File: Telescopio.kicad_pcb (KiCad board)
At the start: 2 copper layers, 201.9 x 119.4 mm, 18 parts, among them CON1 BARREL_JACK, P1 CONN_01X03, P10 CONN_01X08, P12 CONN_01X04, P13 CONN_01X04, P2 CONN_01X03, P3 CONN_01X05, P4 CONN_01X19, P5 CONN_01X19, P50 CONN_01X04, P51 CONN_01X10, P7 CONN_01X08, P8 CONN_01X08, P9 CONN_01X08

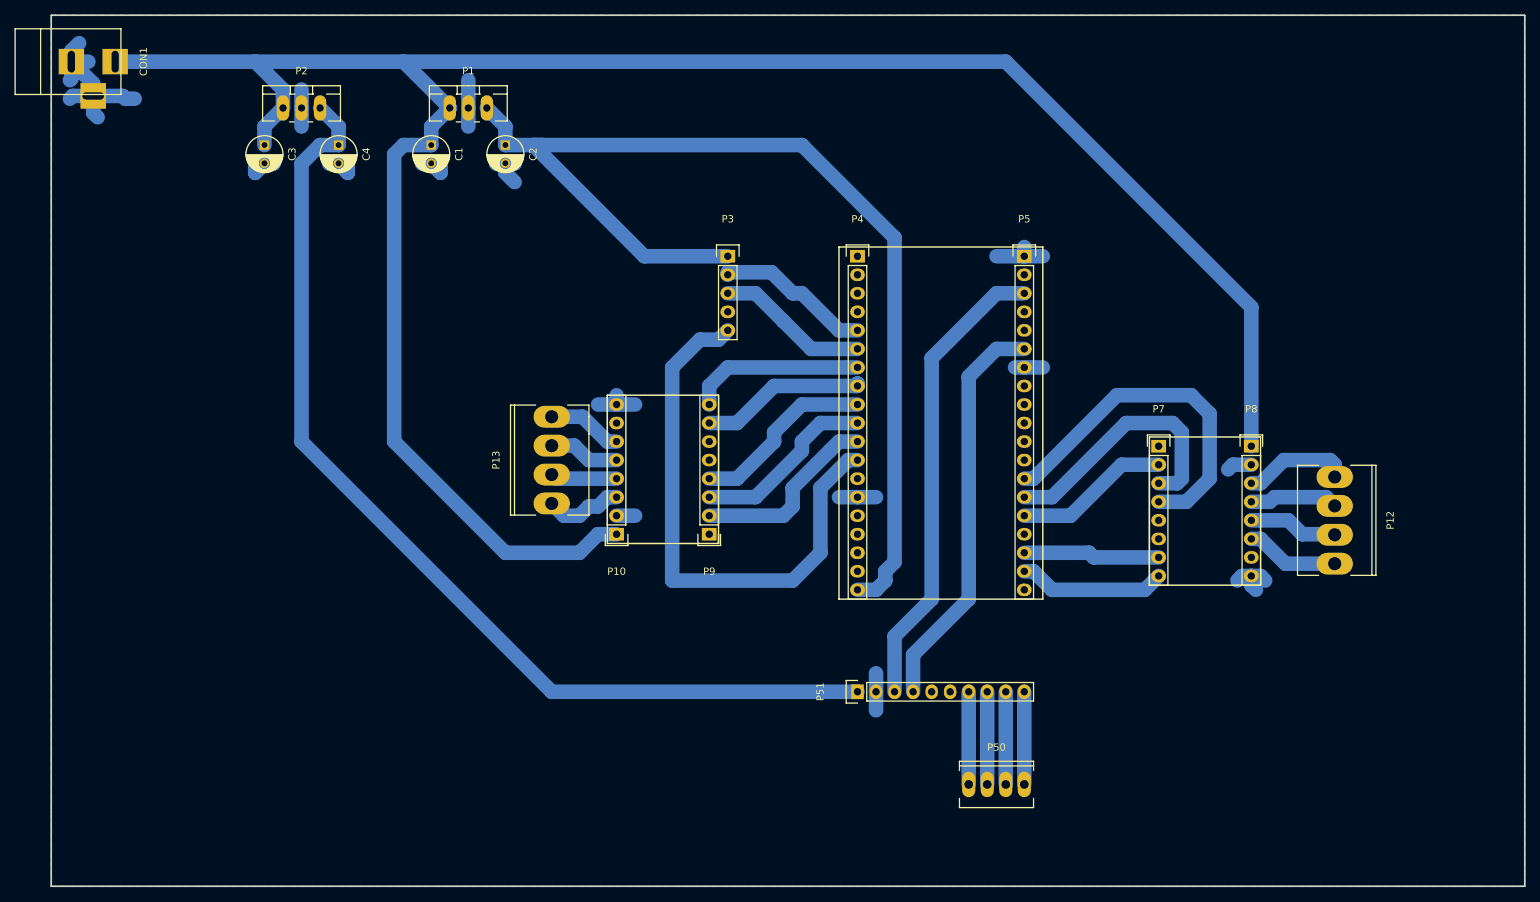
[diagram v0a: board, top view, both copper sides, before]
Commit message: button reset
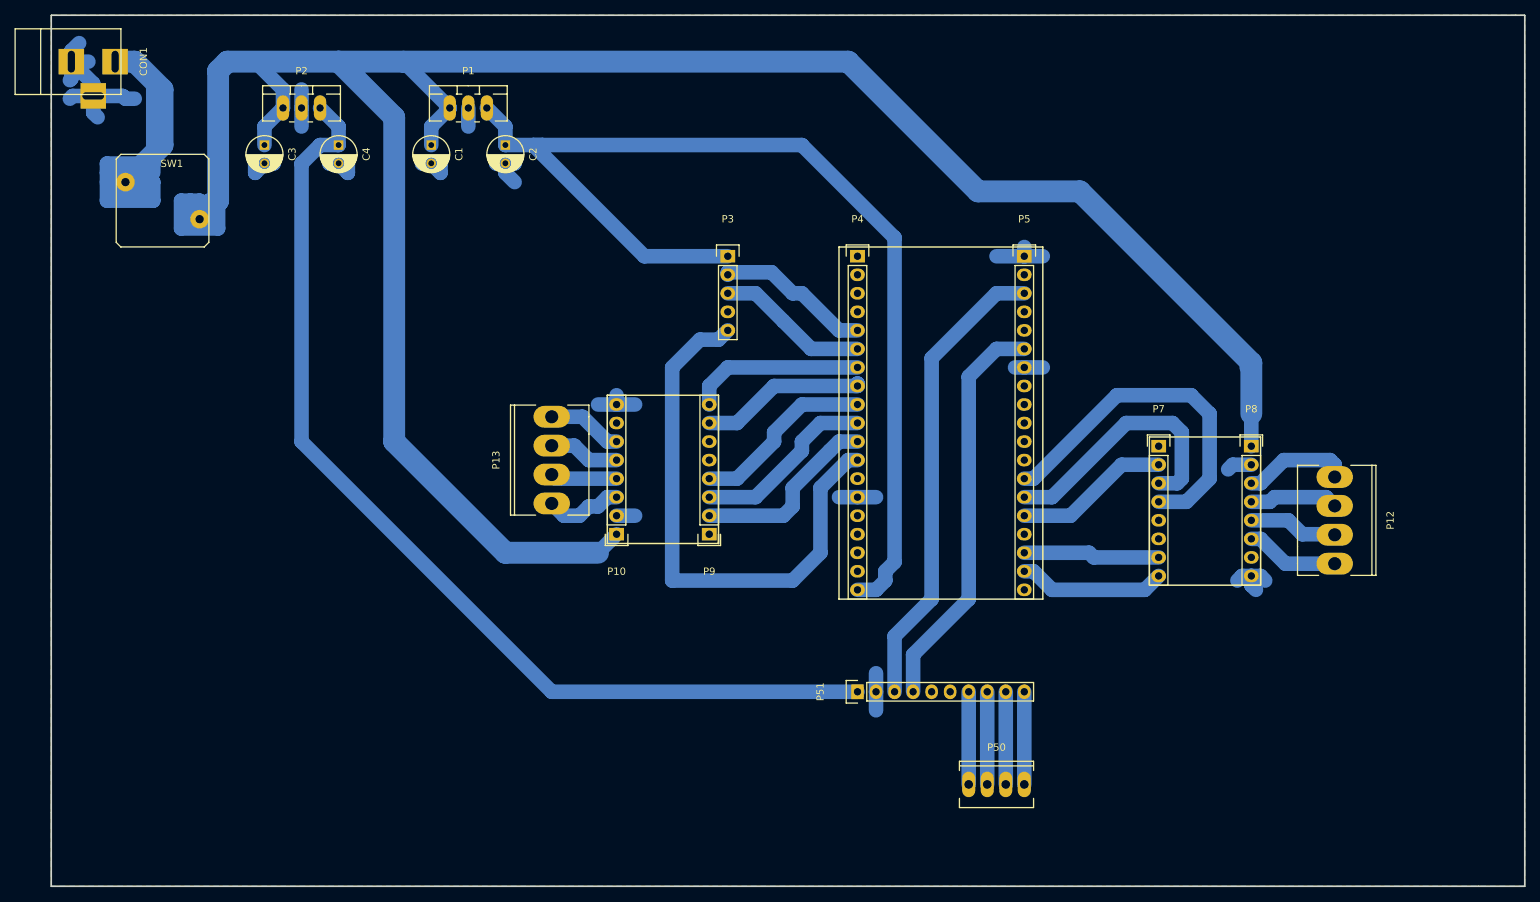
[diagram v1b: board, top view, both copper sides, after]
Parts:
- added SW1: SW_PUSH, Buttons_Switches_ThroughHole:SW_PUSH, F.Cu at (35.6, 53.3)
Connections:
- C1 pad 1: /24v -> /24v_Sal
- C3 pad 1: /24v -> /24v_Sal
- P1 pad 1: /24v -> /24v_Sal
- P10 pad 1: /24v -> /24v_Sal
- P2 pad 1: /24v -> /24v_Sal
- P8 pad 1: /24v -> /24v_Sal
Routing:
- net /24v_Sal: track 0.00 -> 373.3 mm
- net /24v: track 300.7 -> 80.6 mm
- net GND: track 100.8 -> 97.0 mm

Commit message: modifed pcb for testing
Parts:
- removed C1, C2, C3, C4: C, Capacitors_ThroughHole:C_Radial_D5_L11_P2.5
- removed CON1: BARREL_JACK, Connect:BARREL_JACK
- removed P1, P2: CONN_01X03, TO_SOT_Packages_THT:TO-220_Neutral123_Vertical_LargePads
- removed P10, P7, P8, P9: CONN_01X08, Pin_Headers:Pin_Header_Straight_1x08
- removed P12, P13: CONN_01X04, Sockets_MOLEX_KK-System:Socket_MOLEX-KK-RM3-96mm_Lock_4pin_straight
- removed P3: CONN_01X05, Pin_Headers:Pin_Header_Straight_1x05
- removed P50: CONN_01X04, Sockets_MOLEX_KK-System:Socket_MOLEX-KK-RM2-54mm_Lock_4pin_straight
- removed P51: CONN_01X10, Pin_Headers:Pin_Header_Straight_1x10
- removed SW1: SW_PUSH, Buttons_Switches_ThroughHole:SW_PUSH
- added H1: Temp_humidity, Pin_Headers:Pin_Header_Straight_1x04, F.Cu at (107.3, 57.8)
- added J1: ScaleL, Pin_Headers:Pin_Header_Straight_1x04, F.Cu at (166.4, 68.7)
- added J2: Scale, Pin_Headers:Pin_Header_Straight_1x06, F.Cu at (186.8, 66.2)
- added S1: Shifter, Pin_Headers:Pin_Header_Straight_1x06, F.Cu at (104.5, 83.4)
- added S2: ShifterR, Pin_Headers:Pin_Header_Straight_1x06, F.Cu at (117.2, 83.2)
- added Z1: Buzzer, Pin_Headers:Pin_Header_Straight_1x02, F.Cu at (141.7, 107.8)
- added Z2: Motor, Pin_Headers:Pin_Header_Straight_1x02, F.Cu at (112.0, 94.1)
- P4: value CONN_01X19 -> ESP_32
- P5: value CONN_01X19 -> esp_lora
- moved P5 39.0 mm to (158.3, 99.7), turned to 180 degrees
- moved P4 8.40 mm to (135.4, 53.9)
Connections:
- P4 pad 1: (no net) -> /GND2
- P4 pad 10: /M1_2 -> Net-(P4-Pad10)
- P4 pad 11: /M0_2 -> /SCL
- P4 pad 12: /INT_IMU -> Net-(P4-Pad12)
- P4 pad 13: (no net) -> Net-(P4-Pad13)
- P4 pad 14: GND -> Net-(P4-Pad14)
- P4 pad 15: (no net) -> Net-(P4-Pad15)
- P4 pad 16: (no net) -> Net-(P4-Pad16)
- P4 pad 17: (no net) -> Net-(P4-Pad17)
- P4 pad 18: (no net) -> /SDA
- P4 pad 19: /5v -> Net-(P4-Pad19)
- P4 pad 2: (no net) -> /5v1
- P4 pad 3: (no net) -> /3v
- P4 pad 4: (no net) -> /GND
- P4 pad 5: /SCL_2 -> Net-(P4-Pad5)
- P4 pad 6: /SDA_2 -> Net-(P4-Pad6)
- P4 pad 7: /Dir_2 -> Net-(P4-Pad7)
- P4 pad 8: /Step_2 -> /M0
- P4 pad 9: /M2_2 -> Net-(P4-Pad9)
- P5 pad 1: GND -> /DT
- P5 pad 10: (no net) -> Net-(P5-Pad10)
- P5 pad 11: (no net) -> Net-(P5-Pad11)
- P5 pad 12: (no net) -> Net-(P5-Pad12)
- P5 pad 13: /M2_1 -> Net-(P5-Pad13)
- P5 pad 14: /M1_1 -> Net-(P5-Pad14)
- P5 pad 15: /M0_1 -> Net-(P5-Pad15)
- P5 pad 16: (no net) -> Net-(P5-Pad16)
- P5 pad 17: /Step_1 -> Net-(P5-Pad17)
- P5 pad 18: /Dir_1 -> /VCC
- P5 pad 19: (no net) -> /GND1
- P5 pad 2: (no net) -> Net-(P5-Pad2)
- P5 pad 3: /SCL -> /SCK
- P5 pad 4: (no net) -> Net-(P5-Pad4)
- P5 pad 5: (no net) -> Net-(P5-Pad5)
- P5 pad 6: /SDA -> Net-(P5-Pad6)
- P5 pad 7: GND -> Net-(P5-Pad7)
- P5 pad 8: (no net) -> Net-(P5-Pad8)
- P5 pad 9: (no net) -> Net-(P5-Pad9)
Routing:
- net /24v_Sal: track 373.3 -> 0.00 mm
- net /5v: track 150.8 -> 0.00 mm
- net /3v3: track 140.8 -> 0.00 mm
- net /GND: track 0.00 -> 101.2 mm
- net GND: track 97.0 -> 0.00 mm
- net /GND1: track 0.00 -> 89.4 mm
- net /24v: track 80.6 -> 0.00 mm
- net /INT_IMU: track 76.4 -> 0.00 mm
- net /5v1: track 0.00 -> 51.0 mm
- net /M2_1: track 48.4 -> 0.00 mm
- net /SDA: track 55.5 -> 97.1 mm
- net /M1_1: track 36.1 -> 0.00 mm
- net /DT: track 0.00 -> 32.3 mm
- net /GND2: track 0.00 -> 29.7 mm
- net /SCK: track 0.00 -> 28.1 mm
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- removed copper zone on B.Cu, net GND
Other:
- board size 201.9 x 119.4 mm -> 100.3 x 58.4 mm

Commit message: change label name
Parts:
- Z2: value Motor -> Relay
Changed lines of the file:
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@@
       (effects (font (size 1 1) (thickness 0.15)))
     )
-    (fp_text value Motor (at 0 -3.1 270) (layer F.Fab)
+    (fp_text value Relay (at 0 -3.1 270) (layer F.Fab)
       (effects (font (size 1 1) (thickness 0.15)))
     )

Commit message: general fixes
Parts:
- moved Z1 8.74 mm to (133.6, 104.6)
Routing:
- net /GND: track 101.2 -> 15.2 mm
- net /GND1: track 89.4 -> 36.3 mm
- net /5v1: track 51.0 -> 63.9 mm
- net Net-(P5-Pad2): track 23.2 -> 27.8 mm
- net /3v: track 27.0 -> 25.0 mm
- net /M0: track 25.7 -> 24.1 mm
- net /SCK: track 28.1 -> 29.7 mm
- net /VCC: track 16.7 -> 17.3 mm
- added copper zone on B.Cu, net /GND
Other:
- board size 100.3 x 58.4 mm -> 99.6 x 60.5 mm

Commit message: general fixes
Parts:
- added M1: Conn_01x09, Pin_Headers:Pin_Header_Straight_1x09, F.Cu at (141.2, 120.3)
- added S3: Conn_01x06, Pin_Headers:Pin_Header_Straight_1x06, F.Cu at (141.2, 120.3)
- Z2: value Relay -> Motor
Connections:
- H1 pad 1: /GND2 -> /GND
- J1 pad 4: /GND1 -> /GND
- J2 pad 1: Net-(J2-Pad1) -> (no net)
- J2 pad 2: Net-(J2-Pad2) -> (no net)
- J2 pad 3: /A+ -> (no net)
- J2 pad 4: /A- -> (no net)
- J2 pad 5: /E- -> (no net)
- J2 pad 6: /E+ -> (no net)
- P4 pad 1: /GND2 -> /GND
- P4 pad 10: Net-(P4-Pad10) -> (no net)
- P4 pad 12: Net-(P4-Pad12) -> (no net)
- P4 pad 13: Net-(P4-Pad13) -> (no net)
- P4 pad 14: Net-(P4-Pad14) -> (no net)
- P4 pad 15: Net-(P4-Pad15) -> (no net)
- P4 pad 16: Net-(P4-Pad16) -> (no net)
- P4 pad 17: Net-(P4-Pad17) -> (no net)
- P4 pad 19: Net-(P4-Pad19) -> (no net)
- P4 pad 5: Net-(P4-Pad5) -> (no net)
- P4 pad 6: Net-(P4-Pad6) -> (no net)
- P4 pad 7: Net-(P4-Pad7) -> (no net)
- P4 pad 9: Net-(P4-Pad9) -> (no net)
- P5 pad 10: Net-(P5-Pad10) -> (no net)
- P5 pad 11: Net-(P5-Pad11) -> (no net)
- P5 pad 12: Net-(P5-Pad12) -> (no net)
- P5 pad 13: Net-(P5-Pad13) -> (no net)
- P5 pad 14: Net-(P5-Pad14) -> (no net)
- P5 pad 15: Net-(P5-Pad15) -> (no net)
- P5 pad 16: Net-(P5-Pad16) -> (no net)
- P5 pad 17: Net-(P5-Pad17) -> (no net)
- P5 pad 19: /GND1 -> /GND
- P5 pad 4: Net-(P5-Pad4) -> (no net)
- P5 pad 5: Net-(P5-Pad5) -> (no net)
- P5 pad 6: Net-(P5-Pad6) -> (no net)
- P5 pad 7: Net-(P5-Pad7) -> (no net)
- P5 pad 8: Net-(P5-Pad8) -> (no net)
- P5 pad 9: Net-(P5-Pad9) -> (no net)
- S1 pad 2: Net-(S1-Pad2) -> (no net)
- S1 pad 3: Net-(S1-Pad3) -> (no net)
- S1 pad 4: Net-(S1-Pad4) -> (no net)
- S1 pad 5: Net-(S1-Pad5) -> (no net)
- S2 pad 2: Net-(S2-Pad2) -> (no net)
- S2 pad 3: Net-(S2-Pad3) -> (no net)
- S2 pad 4: Net-(S2-Pad4) -> (no net)
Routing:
- net /GND: track 15.2 -> 139.9 mm
- net /GND1: track 36.3 -> 0.00 mm
- net /GND2: track 29.7 -> 0.00 mm

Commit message: general fixes
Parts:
- added J3: ScaleOut, Pin_Headers:Pin_Header_Straight_1x06, F.Cu at (193.5, 78.7)
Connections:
- J2 pad 3: (no net) -> /A+
- J2 pad 4: (no net) -> /A-
- J2 pad 5: (no net) -> /E-
- J2 pad 6: (no net) -> /E+
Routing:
- net /GND: track 139.9 -> 73.9 mm
- net /E-: track 0.00 -> 6.87 mm
- net /E+: track 0.00 -> 6.87 mm
- net /A-: track 0.00 -> 6.87 mm
- net /A+: track 0.00 -> 6.87 mm
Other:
- board size 99.6 x 60.5 mm -> 110.7 x 60.5 mm

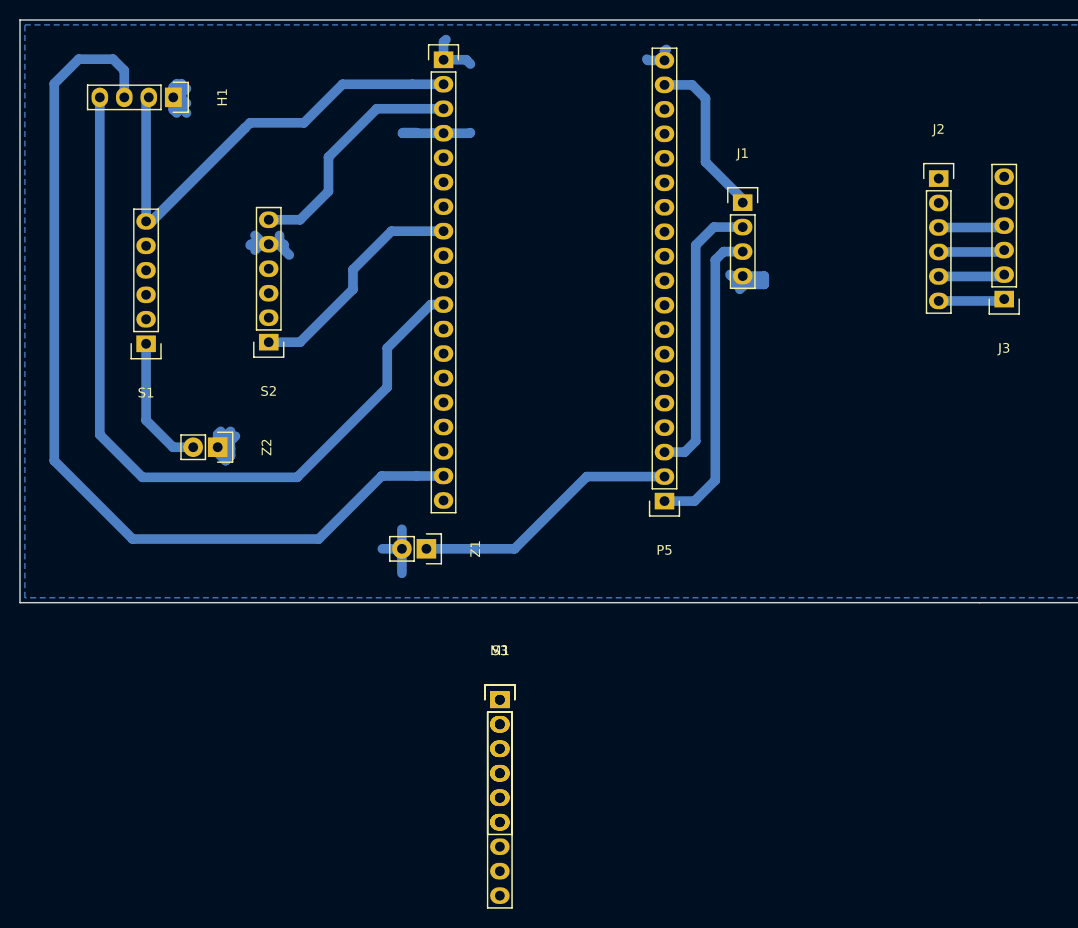
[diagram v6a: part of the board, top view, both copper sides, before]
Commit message: add pinheaders 2.0mm
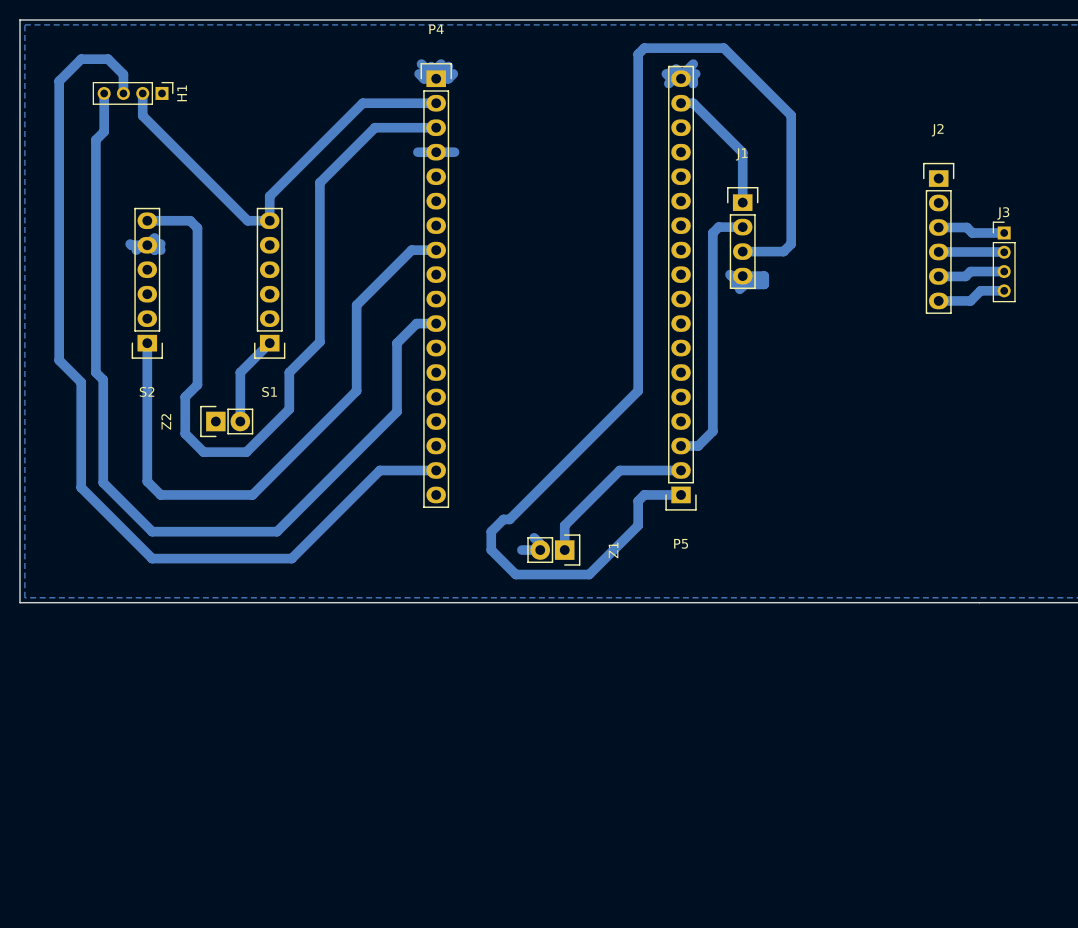
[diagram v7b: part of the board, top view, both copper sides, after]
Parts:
- removed M1: Conn_01x09, Pin_Headers:Pin_Header_Straight_1x09
- removed S3: Conn_01x06, Pin_Headers:Pin_Header_Straight_1x06
- H1: footprint Pin_Headers:Pin_Header_Straight_1x04 -> myelin-kicad:Pin_Header_Straight_1x04_Pitch2.00mm
- J3: value ScaleOut -> CONN_01X04; footprint Pin_Headers:Pin_Header_Straight_1x06 -> myelin-kicad:Pin_Header_Straight_1x04_Pitch2.00mm
- P4: value ESP_32 -> CONN_01X18; footprint Pin_Headers:Pin_Header_Straight_1x19 -> Pin_Headers:Pin_Header_Straight_1x18
- P5: value esp_lora -> CONN_01X18; footprint Pin_Headers:Pin_Header_Straight_1x19 -> Pin_Headers:Pin_Header_Straight_1x18
- moved Z1 14.4 mm to (148.0, 104.8)
- moved S1 12.8 mm to (117.3, 83.3)
- moved S2 12.6 mm to (104.6, 83.3)
- moved J3 6.86 mm to (193.5, 71.9), turned to 0 degrees
- moved Z2 2.67 mm to (111.8, 91.4), turned to 90 degrees
- moved P4 2.11 mm to (134.6, 55.9)
- moved P5 1.83 mm to (160.0, 99.1)
- moved H1 1.24 mm to (106.2, 57.4)
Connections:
- net Net-(P5-Pad2) renamed /B1
- J3 pad 1: /E+ -> /A+
- J3 pad 2: /E- -> /A-
- J3 pad 3: /A- -> /E-
- J3 pad 4: /A+ -> /E+
- P4 pad 17: (no net) -> /SDA
- P4 pad 18: /SDA -> (no net)
- P5 pad 17: (no net) -> /VCC
- P5 pad 18: /VCC -> /GND
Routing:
- net /DT: track 32.2 -> 121.7 mm
- net /3v: track 25.0 -> 80.6 mm
- net /M0: track 24.1 -> 60.6 mm
- net /GND: track 73.9 -> 51.2 mm
- net /5v1: track 63.9 -> 43.8 mm
- net /B1: track 27.8 -> 17.0 mm
- net /SCL: track 82.3 -> 90.8 mm
- net /M1: track 14.0 -> 9.39 mm
- net /VCC: track 17.3 -> 14.1 mm
- net /SCK: track 29.7 -> 27.9 mm
